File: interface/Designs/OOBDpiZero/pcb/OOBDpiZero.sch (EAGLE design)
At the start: 130 parts, among them IC1 LM1117MPX-3.3, IC11 EEPROM24, IC3 DS3231, Q2 12MHz, U1 SN65HVD230(SO8), U2 SN65HVD230(SO8), U4 SY6280, U5 MP1482

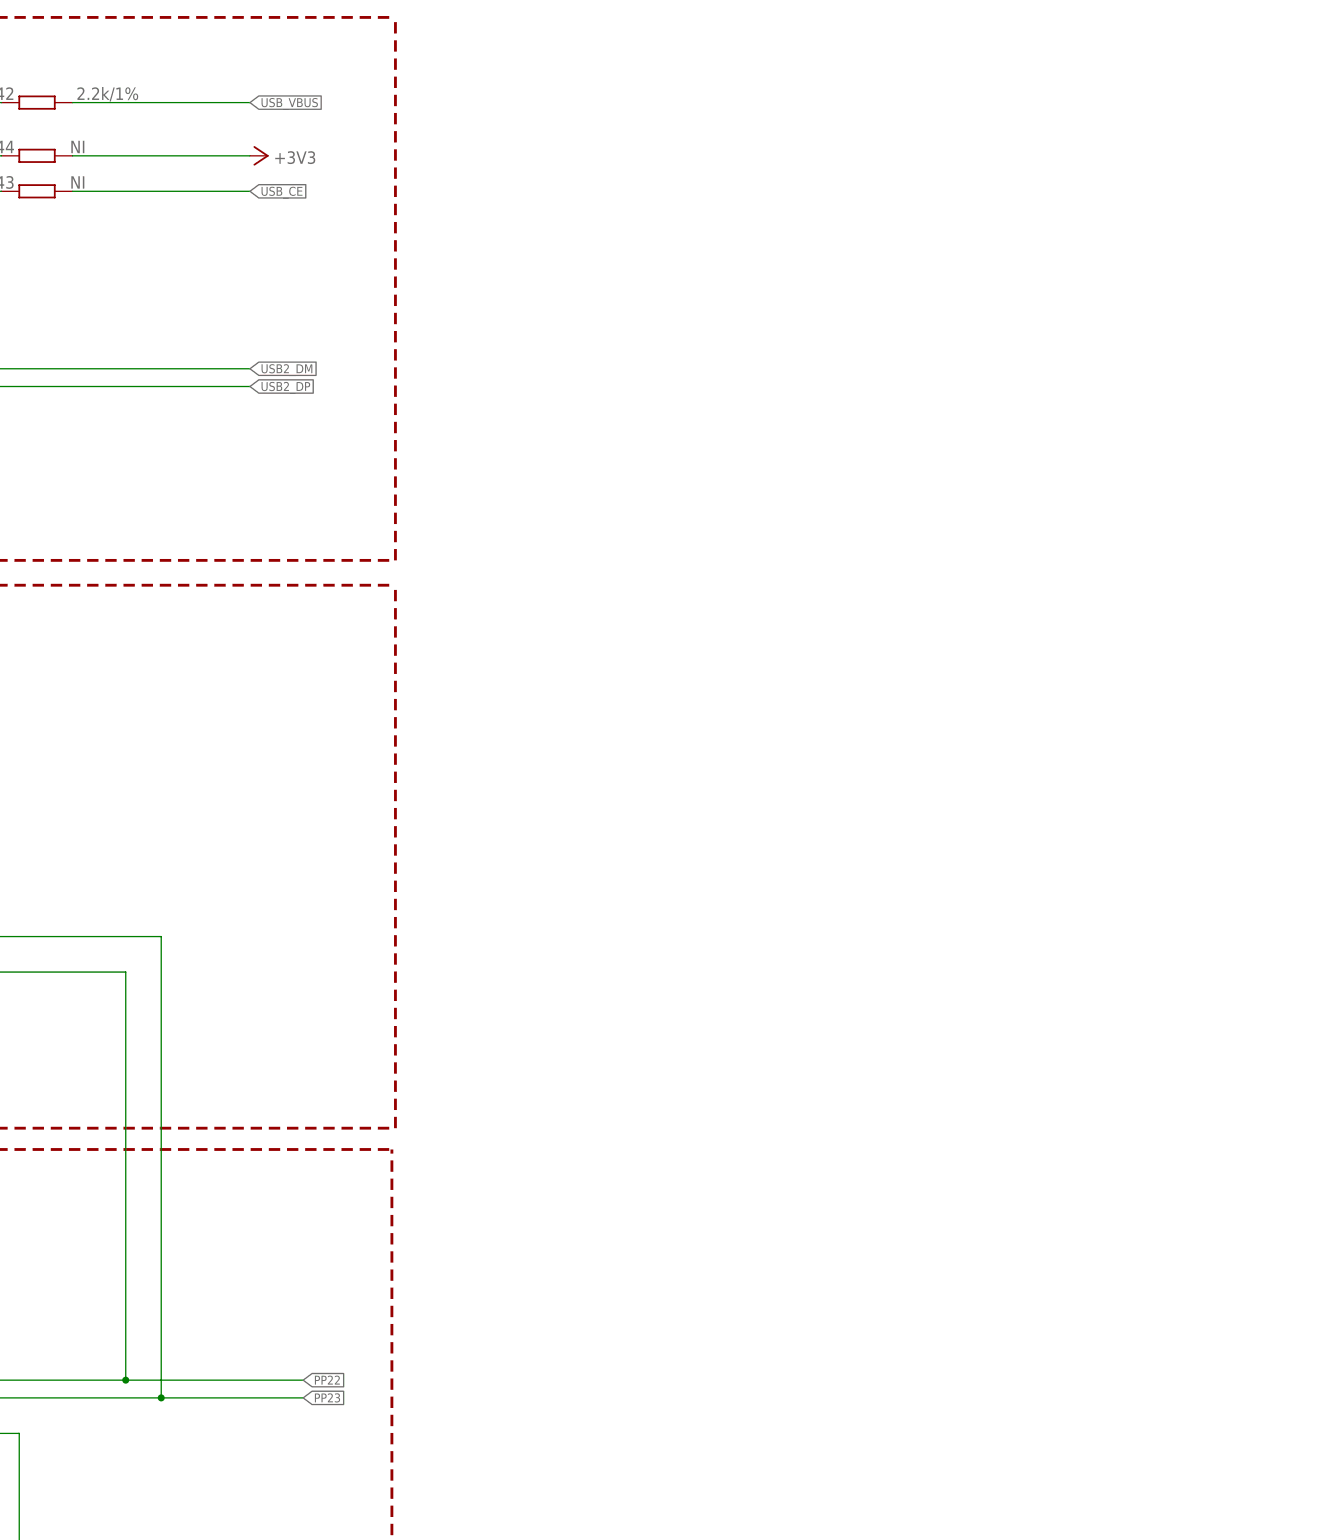
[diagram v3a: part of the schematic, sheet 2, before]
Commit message: PP22/PP23 Pi-Zero USB connection placed and locked add missing OOBD default OBD2-Connector
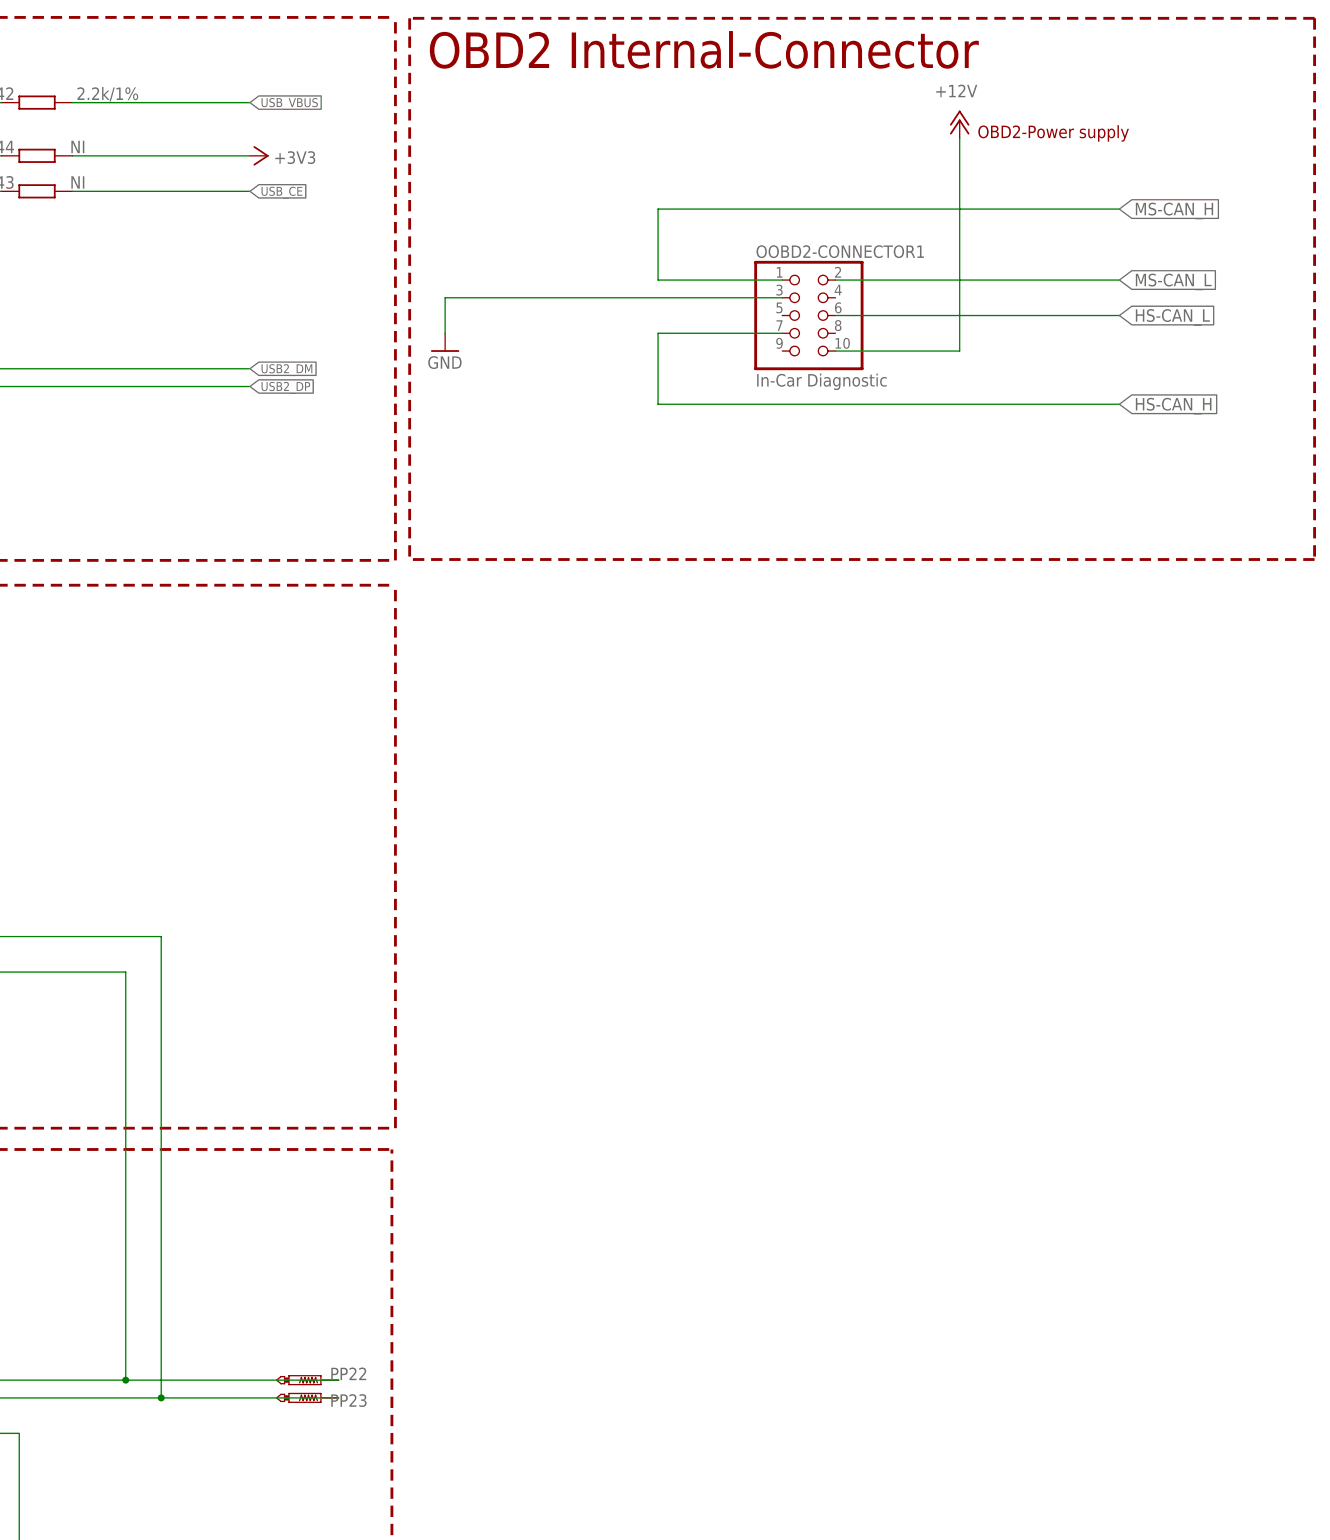
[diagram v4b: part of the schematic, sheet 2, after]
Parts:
- removed JP3: (no value), jumper:JP4E
- added JP5: (no value), jumper:JP1E
- added OOBD2-CONNECTOR1: In-Car Diagnostic, pinhead:PINHD-2X5/90
- added PP22, PP23: PTR1PAD1-11, testpad:PTR1PAD1-11
- renumbered HS-CAN to HS-CAN_TERM, MS-CAN to MS-CAN_TERM
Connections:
- net +12V: now also OOBD2-CONNECTOR1.10
- net +3V3: no longer JP3.1
- net GND: now also OOBD2-CONNECTOR1.3; no longer JP3.4
- net HS-CAN_H: now also OOBD2-CONNECTOR1.7
- net HS-CAN_L: now also OOBD2-CONNECTOR1.6
- net MS-CAN_H: now also OOBD2-CONNECTOR1.1
- net MS-CAN_L: now also OOBD2-CONNECTOR1.2
- net PP22: now also PP22.TP
- net PP23: now also PP23.TP
- net SWCLK: now also JP5.2; no longer JP3.3
- net SWDIO: now also JP5.1; no longer JP3.2
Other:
- note added: "OBD2 Internal-Connector"
- note added: "OBD2-Power supply"

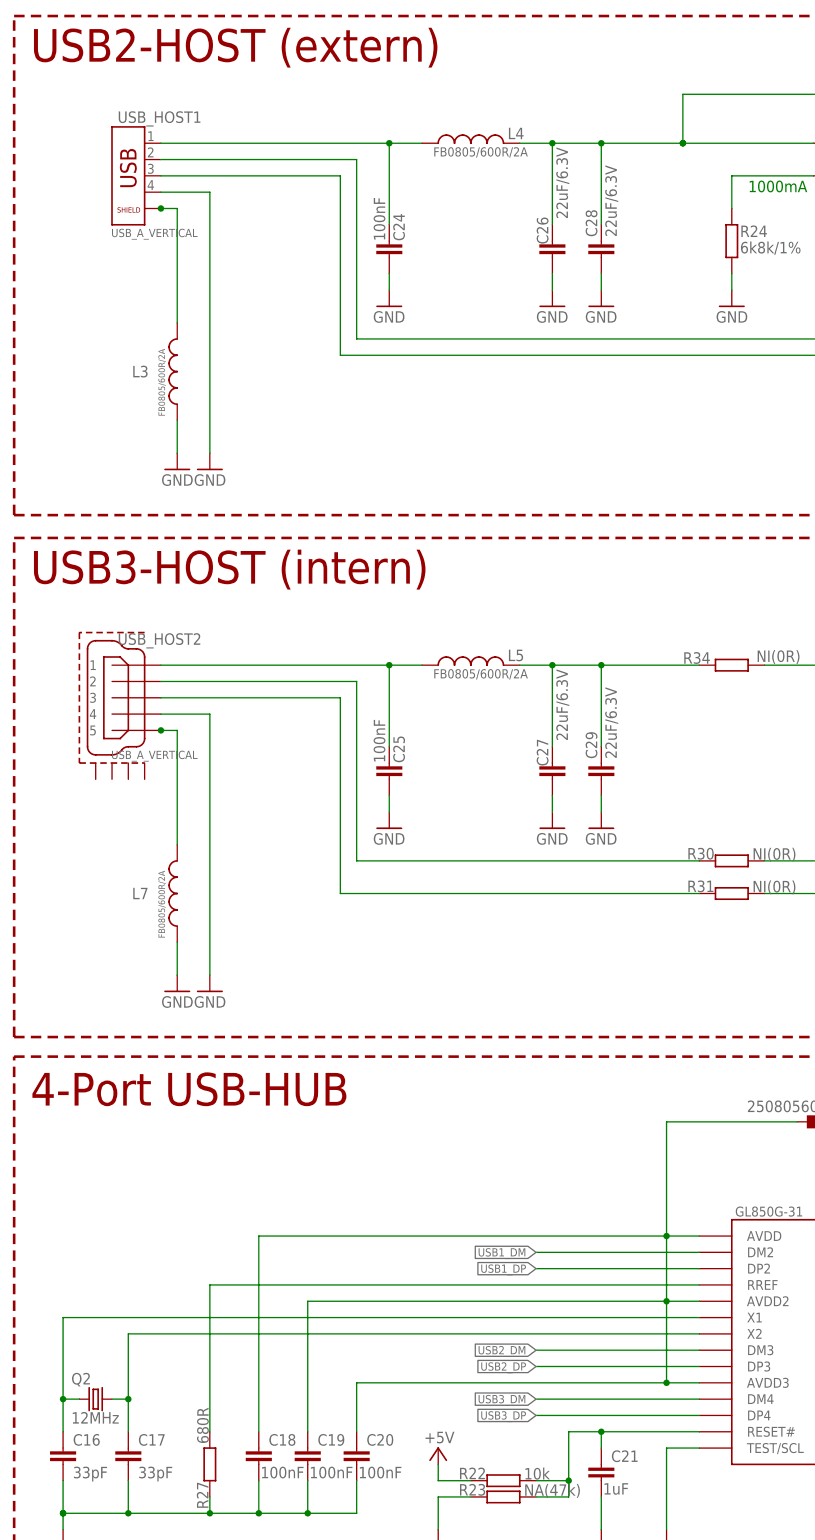
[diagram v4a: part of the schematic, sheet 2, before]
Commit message: - lock position for OOBD2 connector - place all parts on PCB but minor placing optimization necessary as preparation for autorouter
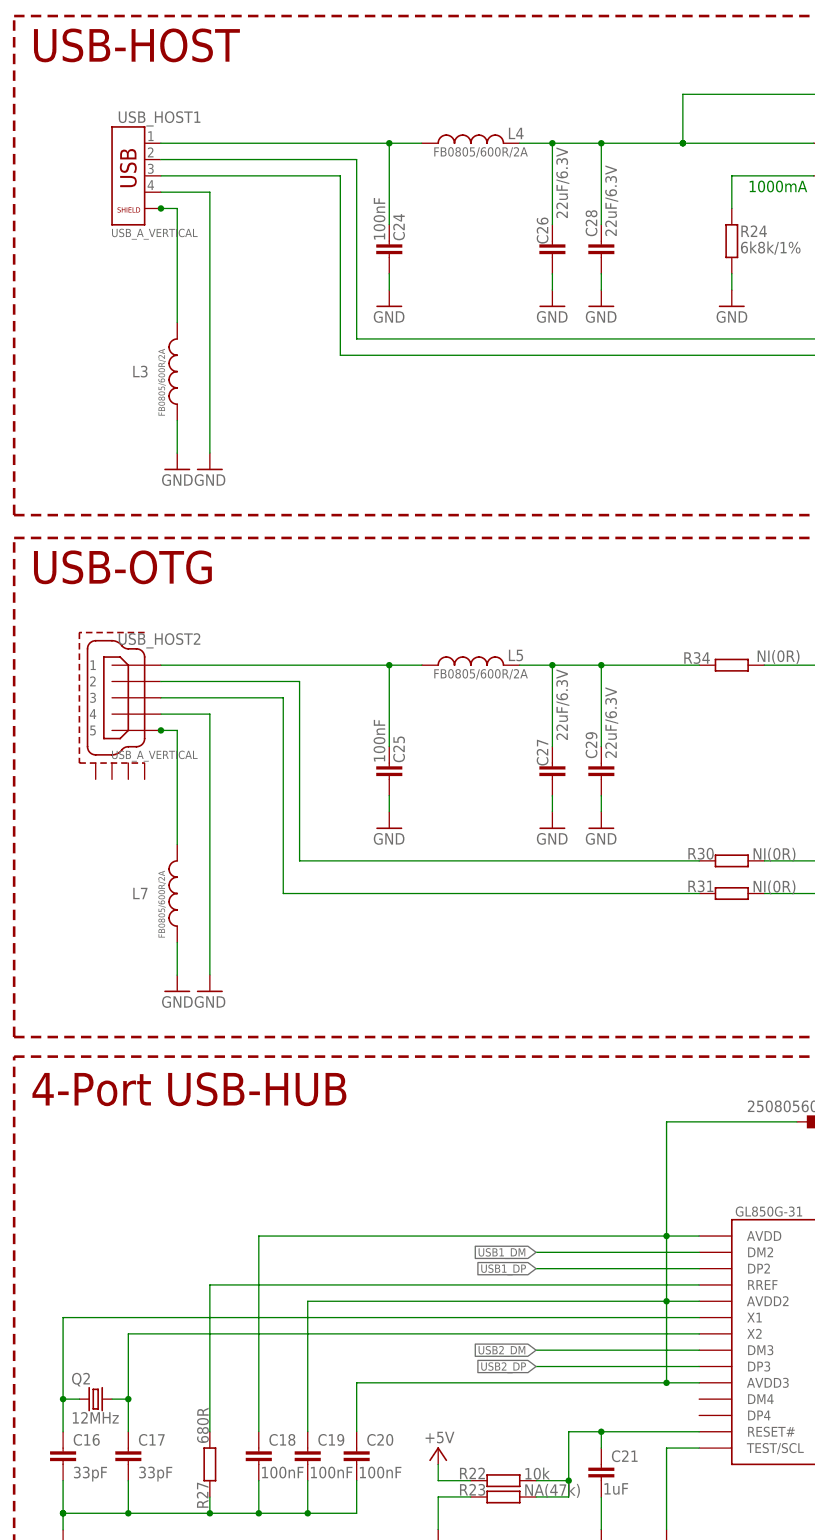
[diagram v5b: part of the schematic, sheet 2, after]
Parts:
- JP1: value (none) -> Audio-Out
- JP2: value (none) -> Prog0_IO
- JP4: value (none) -> UART
- JP5: value (none) -> Prog2_IO
- U3: value (none) -> MAX98357
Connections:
- removed net USB3_DM: R30.1, U$5.DM4, USB_HOST2.2
- removed net USB3_DP: R31.1, U$5.DP4, USB_HOST2.3
- new net N$38: R30.1, USB_HOST2.2
- new net N$43: R31.1, USB_HOST2.3
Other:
- note added: "USB-HOST"
- note added: "USB-OTG"
- note removed: "USB2-HOST (extern)"
- note removed: "USB3-HOST (intern)"
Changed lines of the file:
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@@
 <setting verticaltext="up"/>
 </settings>
-<grid distance="100" unitdist="mil" unit="mil" style="lines" multiple="1" display="yes" altdistance="0.01" altunitdist="inch" altunit="inch"/>
+<grid distance="50" unitdist="mil" unit="mil" style="lines" multiple="1" display="yes" altdistance="0.01" altunitdist="inch" altunit="inch"/>
 <layers>
 <layer number="1" name="Top" color="4" fill="1" visible="no" active="no"/>
@@
 <part name="+3V10" library="supply1" deviceset="+3V3" device=""/>
 <part name="GPIO" library="pizero" deviceset="PIZERO_THROUGH_HOLE" device=""/>
-<part name="U3" library="microbuilder" deviceset="AUDIOAMP_MAX98357" device=""/>
+<part name="U3" library="microbuilder" deviceset="AUDIOAMP_MAX98357" device="" value="MAX98357"/>
 <part name="U$3" library="micro-stm_v3" deviceset="STM32F042C*T" device=""/>
 <part name="P+1" library="supply1" deviceset="+5V" device=""/>
@@
 <part name="C1" library="rcl" deviceset="C-EU" device="C0603K" value="100nF"/>
 <part name="C4" library="rcl" deviceset="C-EU" device="C0805K" value="10uF"/>
-<part name="JP1" library="jumper" deviceset="JP1Q" device=""/>
+<part name="JP1" library="jumper" deviceset="JP1Q" device="" value="Audio-Out"/>
 <part name="GND13" library="supply1" deviceset="GND" device="" value="GND"/>
 <part name="+3V1" library="supply1" deviceset="+3V3" device=""/>
@@
 <part name="C9" library="resistor" deviceset="C-EU" device="C0603" value="100nF"/>
 <part name="R15" library="rcl" deviceset="R-EU_" device="R0603" value="330R"/>
-<part name="JP2" library="jumper" deviceset="JP4E" device=""/>
+<part name="JP2" library="jumper" deviceset="JP4E" device="" value="Prog0_IO"/>
 <part name="+3V5" library="supply1" deviceset="+3V3" device=""/>
 <part name="GND24" library="supply1" deviceset="GND" device="" value="GND"/>
@@
 <part name="GND69" library="supply1" deviceset="GND" device="" value=""/>
 <part name="GND70" library="supply1" deviceset="GND" device="" value=""/>
-<part name="JP4" library="jumper" deviceset="JP2E" device=""/>
+<part name="JP4" library="jumper" deviceset="JP2E" device="" value="UART"/>
 <part name="R44" library="rcl" deviceset="R-EU_" device="R0603" value="NI"/>
 <part name="+3V14" library="supply1" deviceset="+3V3" device=""/>
@@
 <part name="PP22" library="testpad" deviceset="PTR1" device="PAD1-11" value="PTR1PAD1-11"/>
 <part name="PP23" library="testpad" deviceset="PTR1" device="PAD1-11" value="PTR1PAD1-11"/>
-<part name="JP5" library="jumper" deviceset="JP1E" device=""/>
+<part name="JP5" library="jumper" deviceset="JP1E" device="" value="Prog2_IO"/>
 <part name="OOBD2-CONNECTOR1" library="pinhead" deviceset="PINHD-2X5" device="/90" value="In-Car Diagnostic"/>
 <part name="GND28" library="supply1" deviceset="GND" device="" value="GND"/>
@@
 <wire x1="7.62" y1="175.768" x2="7.62" y2="253.492" width="0.4064" layer="94" style="longdash"/>
 <wire x1="249.428" y1="175.768" x2="249.428" y2="253.492" width="0.4064" layer="94" style="longdash"/>
-<text x="10.16" y="246.38" size="5.08" layer="94">USB2-HOST (extern)</text>
+<text x="10.16" y="246.38" size="5.08" layer="94">USB-HOST</text>
 <text x="121.92" y="226.06" size="1.778" layer="91">1000mA</text>
 <wire x1="7.62" y1="94.488" x2="249.428" y2="94.488" width="0.4064" layer="94" style="longdash"/>
@@
 <wire x1="7.62" y1="94.488" x2="7.62" y2="172.212" width="0.4064" layer="94" style="longdash"/>
 <wire x1="249.428" y1="94.488" x2="249.428" y2="172.212" width="0.4064" layer="94" style="longdash"/>
-<text x="10.16" y="165.1" size="5.08" layer="94">USB3-HOST (intern)</text>
+<text x="10.16" y="165.1" size="5.08" layer="94">USB-OTG</text>
 <wire x1="7.62" y1="91.44" x2="248.92" y2="91.44" width="0.4064" layer="94" style="longdash"/>
 <wire x1="7.62" y1="7.62" x2="248.92" y2="7.62" width="0.4064" layer="94" style="longdash"/>
@@
 </segment>
 </net>
-<net name="USB3_DM" class="0">
-<segment>
-<pinref part="U$5" gate="G$1" pin="DM4"/>
-<wire x1="88.9" y1="38.1" x2="114.3" y2="38.1" width="0.1524" layer="91"/>
-<label x="88.9" y="38.1" size="1.27" layer="95" rot="R180" xref="yes"/>
-</segment>
-<segment>
-<pinref part="USB_HOST2" gate="G$1" pin="2"/>
-<wire x1="30.48" y1="149.86" x2="60.96" y2="149.86" width="0.1524" layer="91"/>
-<wire x1="60.96" y1="149.86" x2="60.96" y2="121.92" width="0.1524" layer="91"/>
-<pinref part="R30" gate="G$1" pin="1"/>
-<wire x1="114.3" y1="121.92" x2="60.96" y2="121.92" width="0.1524" layer="91"/>
-</segment>
-</net>
-<net name="USB3_DP" class="0">
-<segment>
-<pinref part="U$5" gate="G$1" pin="DP4"/>
-<wire x1="114.3" y1="35.56" x2="88.9" y2="35.56" width="0.1524" layer="91"/>
-<label x="88.9" y="35.56" size="1.27" layer="95" rot="R180" xref="yes"/>
-</segment>
-<segment>
-<pinref part="USB_HOST2" gate="G$1" pin="3"/>
-<wire x1="30.48" y1="147.32" x2="58.42" y2="147.32" width="0.1524" layer="91"/>
-<wire x1="58.42" y1="147.32" x2="58.42" y2="116.84" width="0.1524" layer="91"/>
-<pinref part="R31" gate="G$1" pin="1"/>
-<wire x1="114.3" y1="116.84" x2="58.42" y2="116.84" width="0.1524" layer="91"/>
-</segment>
-</net>
 <net name="PP23" class="0">
 <segment>
@@
 </segment>
 </net>
+<net name="N$38" class="0">
+<segment>
+<pinref part="R30" gate="G$1" pin="1"/>
+<wire x1="114.3" y1="121.92" x2="52.07" y2="121.92" width="0.1524" layer="91"/>
+<wire x1="52.07" y1="121.92" x2="52.07" y2="149.86" width="0.1524" layer="91"/>
+<pinref part="USB_HOST2" gate="G$1" pin="2"/>
+<wire x1="52.07" y1="149.86" x2="30.48" y2="149.86" width="0.1524" layer="91"/>
+</segment>
+</net>
+<net name="N$43" class="0">
+<segment>
+<pinref part="R31" gate="G$1" pin="1"/>
+<wire x1="114.3" y1="116.84" x2="49.53" y2="116.84" width="0.1524" layer="91"/>
+<wire x1="49.53" y1="116.84" x2="49.53" y2="147.32" width="0.1524" layer="91"/>
+<pinref part="USB_HOST2" gate="G$1" pin="3"/>
+<wire x1="49.53" y1="147.32" x2="30.48" y2="147.32" width="0.1524" layer="91"/>
+</segment>
+</net>
 </nets>
 </sheet>
@@
 </sheet>
 </sheets>
+<errors>
+</errors>
 </schematic>
 </drawing>
